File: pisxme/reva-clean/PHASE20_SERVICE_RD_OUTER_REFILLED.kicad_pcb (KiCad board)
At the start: 6 copper layers, 300 x 180 mm, 80 parts, among them J1 74221-101LF, J2 A70-112-331N126, J3 JAE SM3ZS067U410ABR1000 B-key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, J4 Amphenol 10171746-00021LF USB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, J5 0039300020, J6 0039300020, J7 Raspberry-Pi-5-Compute-Module, Q1 CSD19536KCS, Q2 CSD19536KCS, U1 LM74700QDBVRQ1, U2 LM74700QDBVRQ1, U3 TPSM63606RDLR, U4 TPSM63606RDLR, U5 TPSM63606RDLR, U6 TPD4EUSB30, U7 TUSB9261IPVP, U8 Texas_DRT_3, U9 TPD4EUSB30

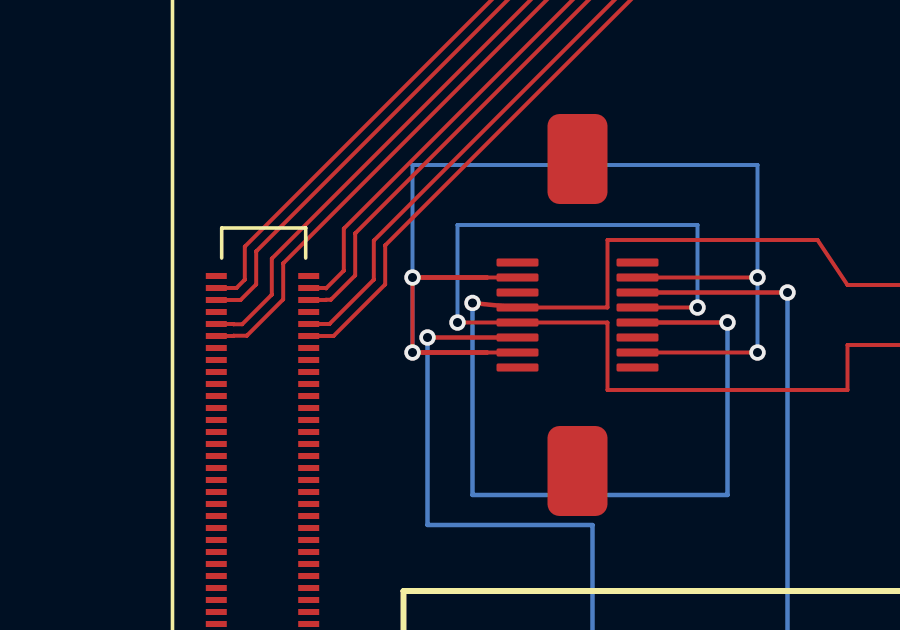
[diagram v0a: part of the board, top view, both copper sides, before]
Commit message: Validate Phase 20 service routing
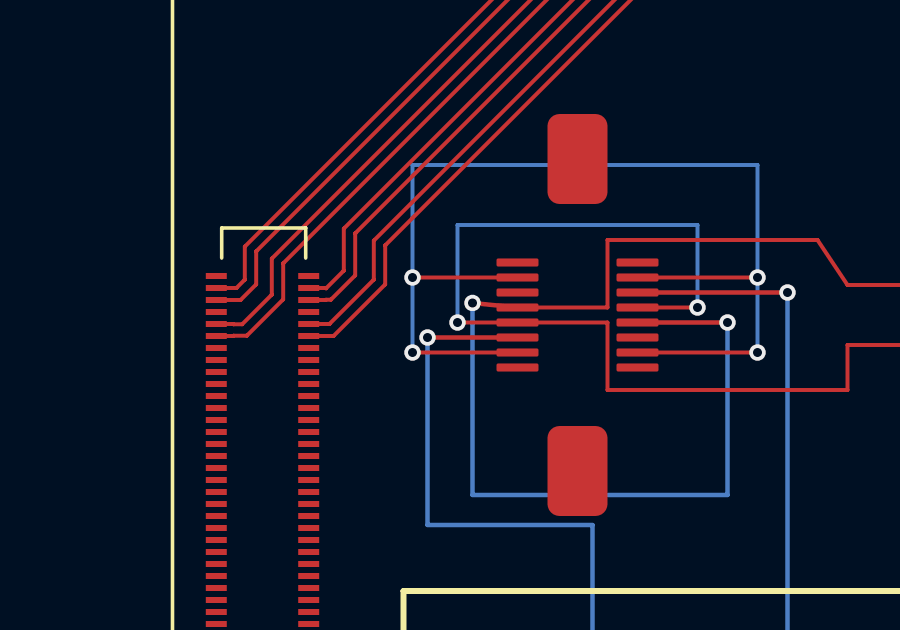
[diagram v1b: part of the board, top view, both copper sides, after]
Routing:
- net /SERVICE/SERVICE_VBUS_SENSE: track 46.5 -> 39.0 mm
